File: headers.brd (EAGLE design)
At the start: 35.5 x 41.3 mm, 15 parts

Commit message: Headers: split C5-6 again, make some TX traces shorter
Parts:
- removed C5-6: 330p, capacitor-wima:C5B2.5
- added C5, C6: 330p, capacitor-wima:C5B2.5
- moved C12 4.84 mm to (9.84, 24.8), turned to 90 degrees
- moved C3 2.86 mm to (27.9, 34.9)
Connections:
- net GND: now also C5.1, C6.1, RXIN.2, RXOUT.2, TXIN.1, TXOUT.2; no longer C5-6.1
- net N$5: now also C5.2, C6.2; no longer C5-6.2
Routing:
- net N$6: track 13.3 -> 9.10 mm
- net N$5: track 19.8 -> 16.4 mm
- net N$1: track 0.00 -> 3.17 mm
- net N$8: track 23.2 -> 20.3 mm
- net N$2: track 10.5 -> 8.82 mm

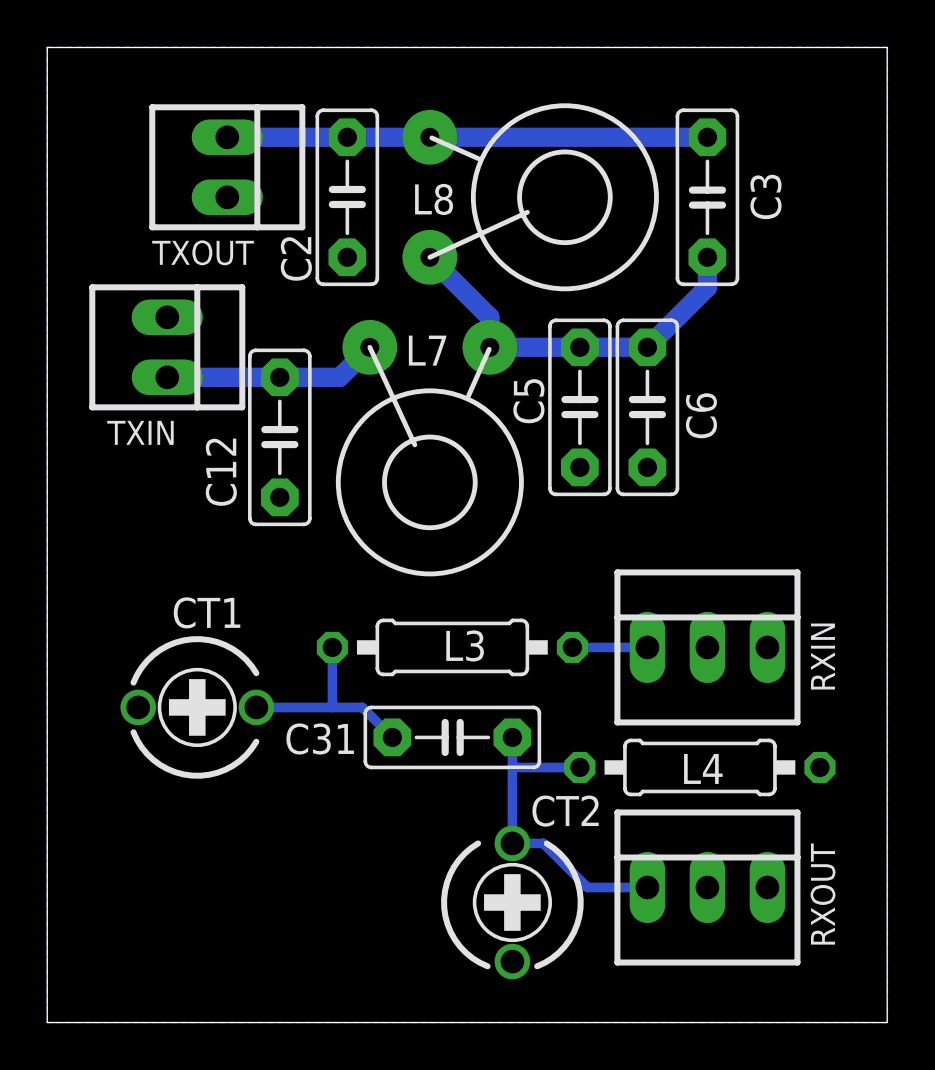
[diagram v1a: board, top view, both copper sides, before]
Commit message: SMT components on the header module
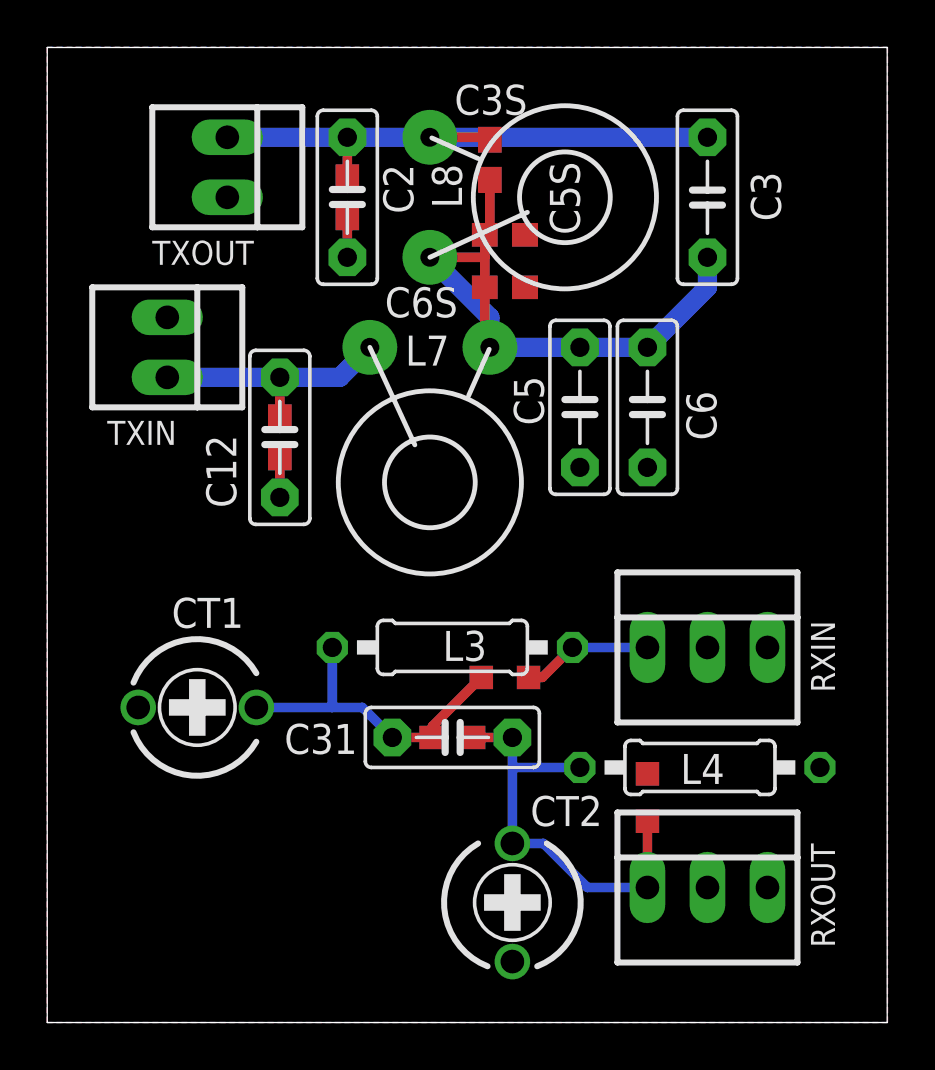
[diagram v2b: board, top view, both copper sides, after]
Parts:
- added C12S, C2S, C31S, C3S, C5S, C6S: (no value), eagle-ltspice:C0603
- added L3S, L4S: (no value), rcl:L2012C
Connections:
- net GND: now also C12S.2, C2S.2, C5S.2, C6S.2, L4S.2
- net N$1: now also L3S.1
- net N$2: now also C31S.1, L3S.2
- net N$4: now also C31S.2, L4S.1
- net N$5: now also C3S.2, C5S.1, C6S.1
- net N$6: now also C12S.1
- net N$8: now also C2S.1, C3S.1
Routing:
- net N$5: track 16.4 -> 26.0 mm
- net N$2: track 8.82 -> 13.9 mm
- net N$4: track 13.8 -> 18.3 mm
- net N$8: track 20.3 -> 24.6 mm
- net GND: track 0.00 -> 3.38 mm
- net N$1: track 3.17 -> 5.56 mm
- net N$6: track 9.10 -> 10.8 mm
- added copper zone on layer 1, net GND
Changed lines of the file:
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@@
 <grid distance="0.3175" unitdist="mm" unit="mm" style="lines" multiple="1" display="yes" altdistance="1.27" altunitdist="mm" altunit="mm"/>
 <layers>
-<layer number="1" name="Top" color="4" fill="1" visible="no" active="yes"/>
-<layer number="16" name="Bottom" color="1" fill="1" visible="yes" active="yes"/>
+<layer number="1" name="Top" color="4" fill="1" visible="yes" active="yes"/>
+<layer number="16" name="Bottom" color="1" fill="1" visible="no" active="yes"/>
 <layer number="17" name="Pads" color="2" fill="1" visible="yes" active="yes"/>
 <layer number="18" name="Vias" color="2" fill="1" visible="yes" active="yes"/>
@@
 <layer number="25" name="tNames" color="7" fill="1" visible="yes" active="yes"/>
 <layer number="26" name="bNames" color="7" fill="1" visible="no" active="yes"/>
-<layer number="27" name="tValues" color="7" fill="1" visible="no" active="yes"/>
+<layer number="27" name="tValues" color="7" fill="1" visible="yes" active="yes"/>
 <layer number="28" name="bValues" color="7" fill="1" visible="no" active="yes"/>
 <layer number="29" name="tStop" color="7" fill="3" visible="no" active="yes"/>
@@
 </element>
 <element name="C2" library="capacitor-wima" package="C5B2.5" value="150p" x="12.7" y="34.925" smashed="yes" rot="R90">
-<attribute name="NAME" x="11.176" y="31.3055" size="1.27" layer="25" ratio="10" rot="R90"/>
+<attribute name="NAME" x="14.224" y="36.322" size="1.27" layer="25" ratio="10" rot="R270"/>
 </element>
 <element name="C3" library="capacitor-wima" package="C5B2.5" value="33p" x="27.94" y="34.925" smashed="yes" rot="R270">
@@
 </element>
 <element name="L8" library="toroids" package="T30-2-28AWG-15T" value="T30-2 / 15T" x="16.1925" y="32.385" smashed="yes" rot="R90">
-<attribute name="NAME" x="17.2825" y="35.47" size="1.27" layer="25" rot="R180"/>
+<attribute name="NAME" x="16.2825" y="36.3325" size="1.27" layer="25" rot="R270"/>
 </element>
 <element name="RXIN" library="con-molex" package="22-23-2031" value="22-23-2031" x="27.94" y="15.875" smashed="yes">
@@
 <element name="C6" library="capacitor-wima" package="C5B2.5" value="330p" x="25.4" y="26.035" smashed="yes" rot="R90">
 <attribute name="NAME" x="28.321" y="24.638" size="1.27" layer="25" ratio="10" rot="R90"/>
+</element>
+<element name="L3S" library="rcl" package="L2012C" value="" x="19.3675" y="14.605" smashed="yes" rot="R180">
+<attribute name="VALUE" x="21.2725" y="17.145" size="1.27" layer="27" rot="R180"/>
+</element>
+<element name="L4S" library="rcl" package="L2012C" value="" x="25.4" y="9.525" smashed="yes" rot="R90">
+<attribute name="VALUE" x="27.94" y="7.62" size="1.27" layer="27" rot="R90"/>
+</element>
+<element name="C31S" library="eagle-ltspice" package="C0603" value="" x="17.145" y="12.065" smashed="yes">
+<attribute name="SPICEMODEL" value="NONE" x="17.145" y="12.065" size="1.778" layer="27" display="off"/>
+<attribute name="SPICEPREFIX" value="C" x="17.145" y="12.065" size="1.778" layer="27" display="off"/>
+<attribute name="VALUE" x="16.51" y="10.16" size="1.27" layer="27"/>
+</element>
+<element name="C3S" library="eagle-ltspice" package="C0603" value="" x="18.7325" y="36.5125" smashed="yes" rot="R270">
+<attribute name="NAME" x="20.32" y="39.6875" size="1.27" layer="25" rot="R180"/>
+<attribute name="SPICEMODEL" value="NONE" x="18.7325" y="36.5125" size="1.778" layer="27" rot="R270" display="off"/>
+<attribute name="SPICEPREFIX" value="C" x="18.7325" y="36.5125" size="1.778" layer="27" rot="R270" display="off"/>
+<attribute name="VALUE" x="16.8275" y="37.1475" size="1.27" layer="27" rot="R270"/>
+</element>
+<element name="C12S" library="eagle-ltspice" package="C0603" value="" x="9.8425" y="24.765" smashed="yes" rot="R270">
+<attribute name="SPICEMODEL" value="NONE" x="9.8425" y="24.765" size="1.778" layer="27" rot="R270" display="off"/>
+<attribute name="SPICEPREFIX" value="C" x="9.8425" y="24.765" size="1.778" layer="27" rot="R270" display="off"/>
+<attribute name="VALUE" x="7.9375" y="25.4" size="1.27" layer="27" rot="R270"/>
+</element>
+<element name="C5S" library="eagle-ltspice" package="C0603" value="" x="19.3675" y="33.3375" smashed="yes">
+<attribute name="NAME" x="22.5425" y="33.3375" size="1.27" layer="25" rot="R90"/>
+<attribute name="SPICEMODEL" value="NONE" x="19.3675" y="33.3375" size="1.778" layer="27" display="off"/>
+<attribute name="SPICEPREFIX" value="C" x="19.3675" y="33.3375" size="1.778" layer="27" display="off"/>
+<attribute name="VALUE" x="18.7325" y="31.4325" size="1.27" layer="27"/>
+</element>
+<element name="C6S" library="eagle-ltspice" package="C0603" value="" x="19.3675" y="31.115" smashed="yes">
+<attribute name="NAME" x="14.2875" y="29.845" size="1.27" layer="25"/>
+<attribute name="SPICEMODEL" value="NONE" x="19.3675" y="31.115" size="1.778" layer="27" display="off"/>
+<attribute name="SPICEPREFIX" value="C" x="19.3675" y="31.115" size="1.778" layer="27" display="off"/>
+<attribute name="VALUE" x="18.7325" y="29.21" size="1.27" layer="27"/>
+</element>
+<element name="C2S" library="eagle-ltspice" package="C0603" value="" x="12.7" y="34.925" smashed="yes" rot="R270">
+<attribute name="SPICEMODEL" value="NONE" x="12.7" y="34.925" size="1.778" layer="27" rot="R270" display="off"/>
+<attribute name="SPICEPREFIX" value="C" x="12.7" y="34.925" size="1.778" layer="27" rot="R270" display="off"/>
+<attribute name="VALUE" x="10.795" y="35.56" size="1.27" layer="27" rot="R270"/>
 </element>
 </elements>
@@
 <wire x1="19.685" y1="7.58" x2="20.995" y2="7.58" width="0.4064" layer="16"/>
 <wire x1="19.685" y1="10.795" x2="19.685" y2="7.58" width="0.4064" layer="16"/>
+<contactref element="L4S" pad="1"/>
+<contactref element="C31S" pad="2"/>
+<wire x1="17.995" y1="12.065" x2="19.685" y2="12.065" width="0.4064" layer="1"/>
+<wire x1="25.4" y1="8.525" x2="25.4" y2="5.715" width="0.4064" layer="1"/>
 </signal>
 <signal name="GND">
@@
 <contactref element="TXOUT" pad="2"/>
 <contactref element="TXIN" pad="1"/>
+<contactref element="L4S" pad="2"/>
+<contactref element="C2S" pad="2"/>
+<contactref element="C5S" pad="2"/>
+<contactref element="C6S" pad="2"/>
+<contactref element="C12S" pad="2"/>
+<wire x1="9.8425" y1="23.915" x2="9.8425" y2="22.225" width="0.4064" layer="1"/>
+<wire x1="12.7" y1="34.075" x2="12.7" y2="32.385" width="0.4064" layer="1"/>
+<polygon width="0.4064" layer="1">
+<vertex x="0" y="0"/>
+<vertex x="35.56" y="0"/>
+<vertex x="35.56" y="41.275"/>
+<vertex x="0" y="41.275"/>
+</polygon>
 </signal>
 <signal name="N$1">
@@
 <contactref element="L3" pad="1"/>
 <wire x1="22.225" y1="15.875" x2="25.4" y2="15.875" width="0.4064" layer="16"/>
+<contactref element="L3S" pad="1"/>
+<wire x1="20.3675" y1="14.605" x2="20.955" y2="14.605" width="0.4064" layer="1"/>
+<wire x1="20.955" y1="14.605" x2="22.225" y2="15.875" width="0.4064" layer="1"/>
 </signal>
 <signal name="N$2">
@@
 <wire x1="12.065" y1="13.335" x2="13.335" y2="13.335" width="0.4064" layer="16"/>
 <wire x1="13.335" y1="13.335" x2="14.605" y2="12.065" width="0.4064" layer="16"/>
+<contactref element="L3S" pad="2"/>
+<contactref element="C31S" pad="1"/>
+<wire x1="14.605" y1="12.065" x2="16.295" y2="12.065" width="0.4064" layer="1"/>
+<wire x1="16.295" y1="12.065" x2="16.295" y2="12.5325" width="0.4064" layer="1"/>
+<wire x1="16.295" y1="12.5325" x2="18.3675" y2="14.605" width="0.4064" layer="1"/>
 </signal>
 <signal name="N$5">
@@
 <wire x1="27.94" y1="32.385" x2="27.94" y2="31.115" width="0.8128" layer="16"/>
 <wire x1="27.94" y1="31.115" x2="25.4" y2="28.575" width="0.8128" layer="16"/>
+<contactref element="C3S" pad="2"/>
+<contactref element="C5S" pad="1"/>
+<contactref element="C6S" pad="1"/>
+<wire x1="18.5175" y1="32.385" x2="18.5175" y2="33.3375" width="0.4064" layer="1"/>
+<wire x1="18.5175" y1="32.385" x2="18.5175" y2="31.115" width="0.4064" layer="1"/>
+<wire x1="18.7325" y1="35.6625" x2="18.7325" y2="33.5525" width="0.4064" layer="1"/>
+<wire x1="18.7325" y1="33.5525" x2="18.5175" y2="33.3375" width="0.4064" layer="1"/>
+<wire x1="16.1925" y1="32.385" x2="18.5175" y2="32.385" width="0.4064" layer="1"/>
+<wire x1="18.5175" y1="31.115" x2="18.5175" y2="28.79" width="0.4064" layer="1"/>
+<wire x1="18.5175" y1="28.79" x2="18.7325" y2="28.575" width="0.4064" layer="1"/>
 </signal>
 <signal name="N$6">
@@
 <wire x1="9.8425" y1="27.305" x2="12.3825" y2="27.305" width="0.8128" layer="16"/>
 <wire x1="12.3825" y1="27.305" x2="13.6525" y2="28.575" width="0.8128" layer="16"/>
+<contactref element="C12S" pad="1"/>
+<wire x1="9.8425" y1="25.615" x2="9.8425" y2="27.305" width="0.4064" layer="1"/>
 </signal>
 <signal name="N$8">
@@
 <wire x1="7.62" y1="37.465" x2="12.7" y2="37.465" width="0.8128" layer="16"/>
 <wire x1="16.1925" y1="37.465" x2="27.94" y2="37.465" width="0.8128" layer="16"/>
+<contactref element="C2S" pad="1"/>
+<contactref element="C3S" pad="1"/>
+<wire x1="12.7" y1="35.775" x2="12.7" y2="37.465" width="0.4064" layer="1"/>
+<wire x1="16.1925" y1="37.465" x2="18.63" y2="37.465" width="0.4064" layer="1"/>
+<wire x1="18.63" y1="37.465" x2="18.7325" y2="37.3625" width="0.4064" layer="1"/>
 </signal>
 </signals>

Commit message: Move SMT components to bottom
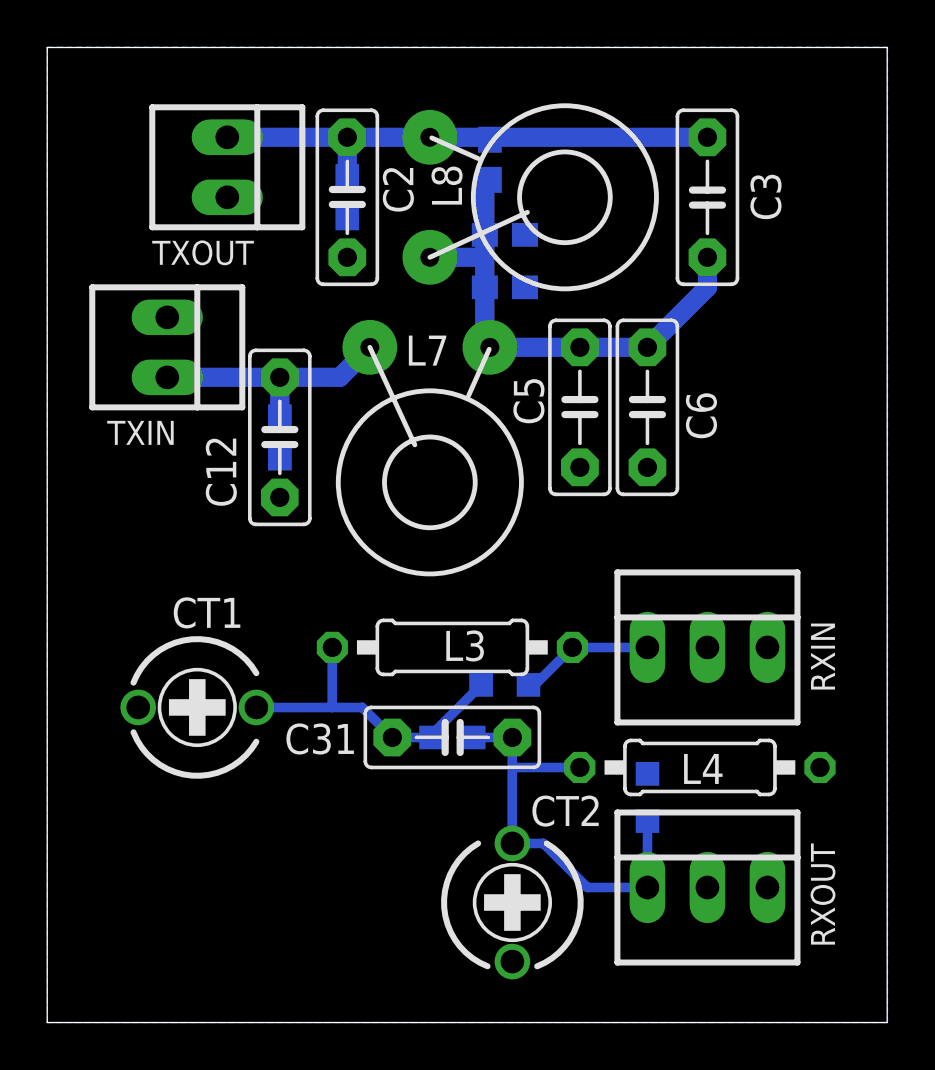
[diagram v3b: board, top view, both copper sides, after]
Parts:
- moved L3S 0.32 mm to (19.4, 14.3), flipped to the bottom, turned to 0 degrees
- flipped C12S to the bottom
- flipped C2S to the bottom
- flipped C31S to the bottom, turned to 180 degrees
- flipped C3S to the bottom
- flipped C5S to the bottom, turned to 180 degrees
- flipped C6S to the bottom, turned to 180 degrees
- flipped L4S to the bottom
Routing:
- net N$5: track 26.0 -> 21.4 mm
- net GND: track 3.38 -> 0.00 mm
- net N$8: track 24.6 -> 22.3 mm
- removed copper zone on layer 1, net GND
